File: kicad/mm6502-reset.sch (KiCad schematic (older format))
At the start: 19 parts, among them SW1 SW_Push, U1 W65C02SxP, U2 AT28C256, U3 62256, U4 W65C22SxP, U5 74HC00, U5 LM555, X1 1MHz

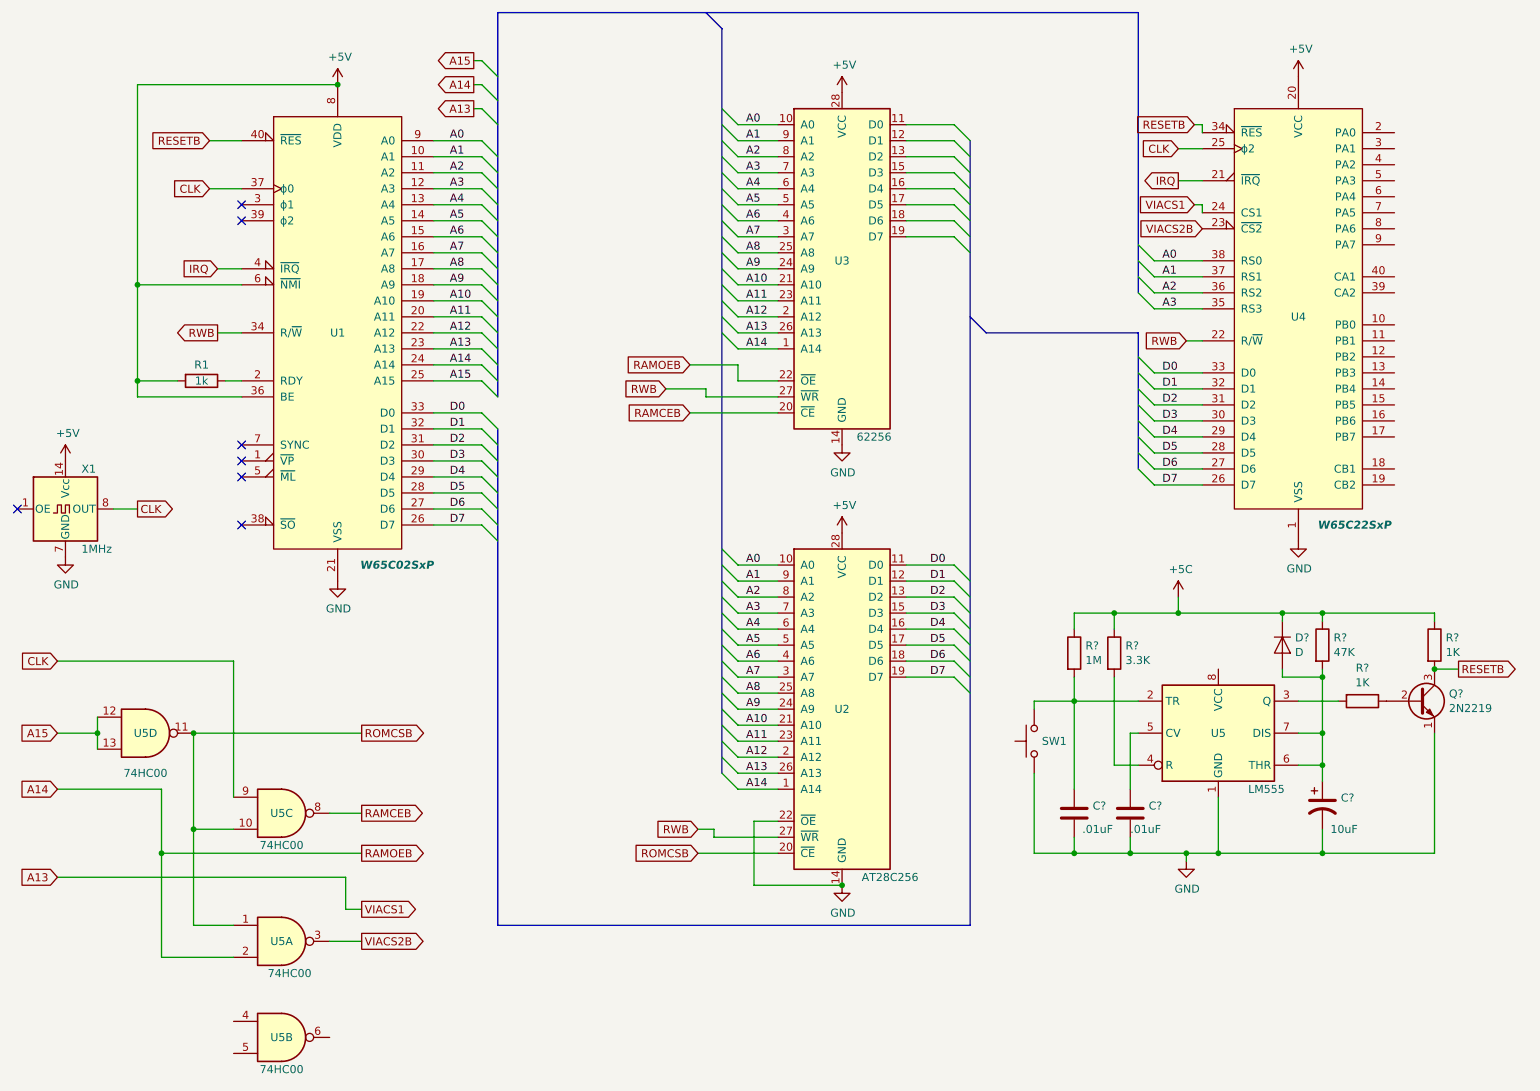
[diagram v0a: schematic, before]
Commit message: Add reset circuit
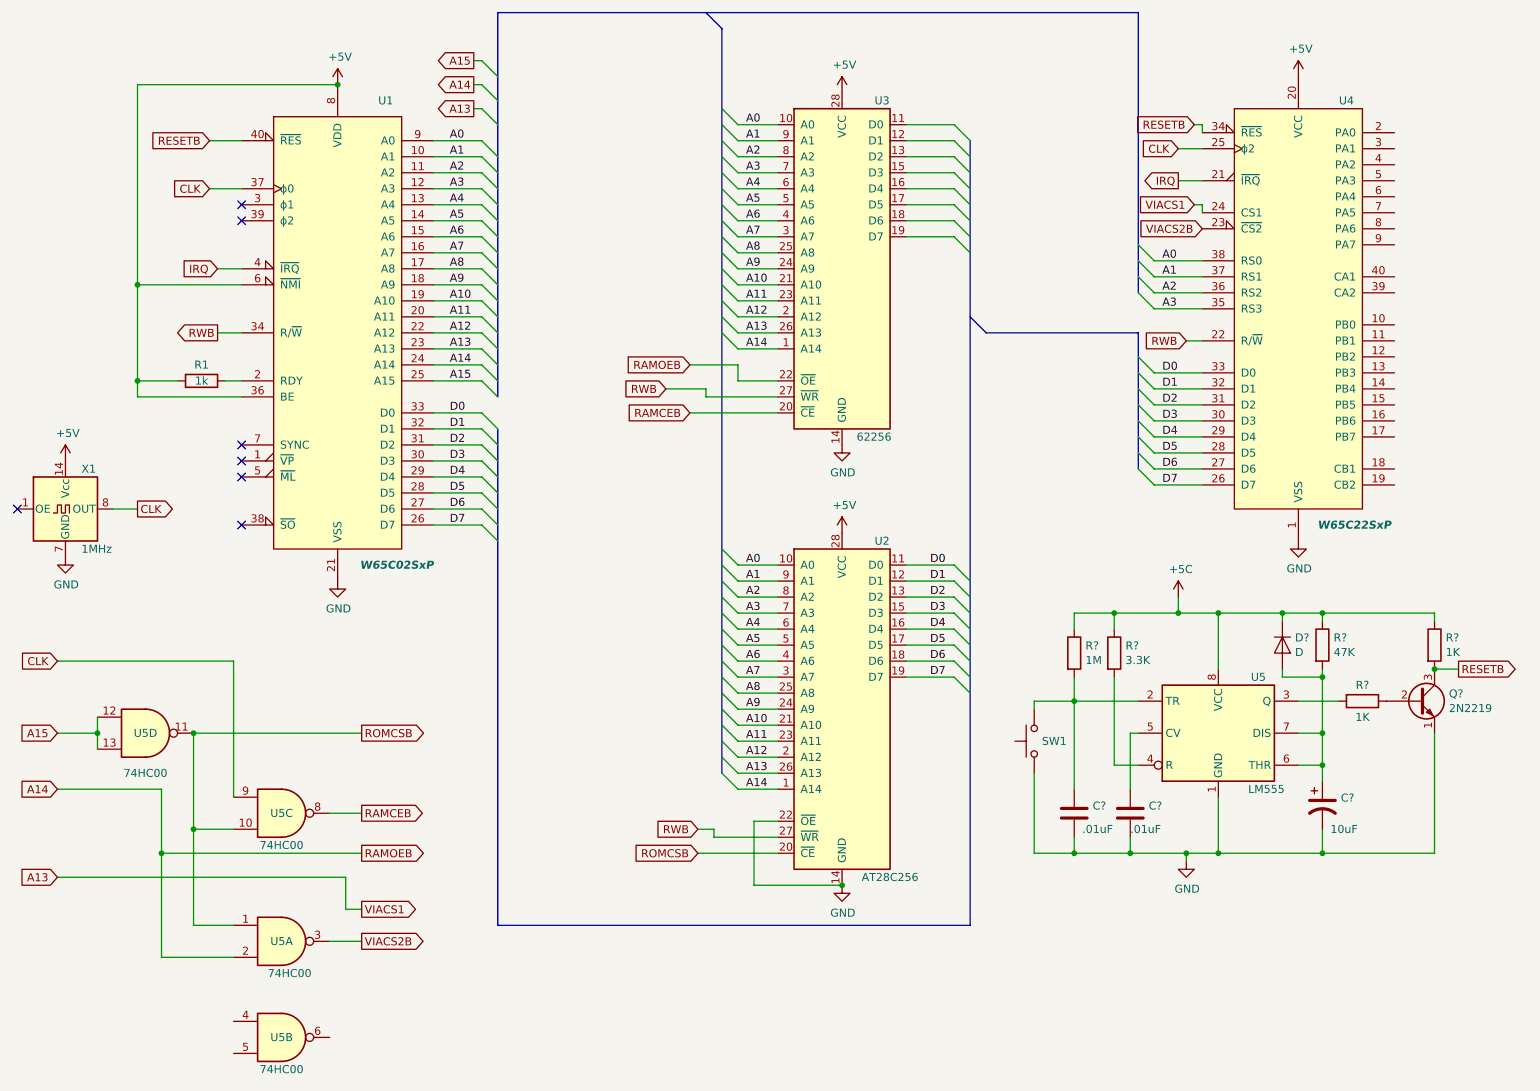
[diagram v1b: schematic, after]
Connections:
- net +5C: now also U5.8 (VCC)
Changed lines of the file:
@@
 U 1 1 63C25691
 P 6250 5250
-F 0 "U2" H 6250 5250 50  0000 C CNN
+F 0 "U2" H 6500 6300 50  0000 C CNN
 F 1 "AT28C256" H 6550 4200 50  0000 C CNN
 F 2 "" H 6250 5250 50  0001 C CNN
@@
 U 1 1 63C2336B
 P 9100 2750
-F 0 "U4" H 9100 2700 50  0000 C CNN
+F 0 "U4" H 9400 4050 50  0000 C CNN
 F 1 "W65C22SxP" H 9450 1400 50  0000 C CIB
 F 2 "" H 9100 2900 50  0001 C CNN
@@
 U 1 1 63C274DB
 P 6250 2500
-F 0 "U3" H 6250 2550 50  0000 C CNN
+F 0 "U3" H 6500 3550 50  0000 C CNN
 F 1 "62256" H 6450 1450 50  0000 C CNN
 F 2 "" H 6250 2500 50  0001 C CNN
@@
 U 1 1 63C201B7
 P 3100 2900
-F 0 "U1" H 3100 2900 50  0000 C CNN
+F 0 "U1" H 3400 4350 50  0000 C CNN
 F 1 "W65C02SxP" H 3700 1450 50  0000 R CIB
 F 2 "" H 3100 4900 50  0001 C CNN
@@
 U 1 1 63CC6136
 P 8600 5400
-F 0 "U5" H 8600 5400 50  0000 C CNN
+F 0 "U5" H 8850 5750 50  0000 C CNN
 F 1 "LM555" H 8900 5050 50  0000 C CNN
 F 2 "" H 8600 5400 50  0001 C CNN
@@
 U 1 1 63CD04BA
 P 9500 5200
-F 0 "R?" V 9293 5200 50  0000 C CNN
-F 1 "1K" V 9384 5200 50  0000 C CNN
+F 0 "R?" V 9400 5200 50  0000 C CNN
+F 1 "1K" V 9600 5200 50  0000 C CNN
 F 2 "" V 9430 5200 50  0001 C CNN
 F 3 "~" H 9500 5200 50  0001 C CNN
@@
 Connection ~ 8350 4650
 Wire Wire Line
-	8350 4650 9000 4650
+	8350 4650 8600 4650
 Wire Wire Line
 	9000 4700 9000 4650
@@
 	10100 5000 9950 5000
 Connection ~ 9950 5000
+Wire Wire Line
+	8600 5000 8600 4650
 Wire Bus Line
 	4100 900  8100 900
@@
 Wire Bus Line
 	5500 1000 5500 5650
+Connection ~ 8600 4650
+Wire Wire Line
+	8600 4650 9000 4650
 $EndSCHEMATC

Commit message: Multiple sheets
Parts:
- removed R1: 1k, symbol Device:R
- removed U1: W65C02SxP, symbol 65xx:W65C02SxP
- removed U2: AT28C256, symbol 8bits:AT28C256
- removed U3: 62256, symbol 8bits:62256
- removed U4: W65C22SxP, symbol 65xx:W65C22SxP
- removed U5: 74HC00, symbol 74xx:74HC00
- removed unit 2 of U5
- removed unit 3 of U5
- removed unit 4 of U5
- removed X1: 1MHz, Oscillator:Oscillator_SeikoEpson_SG-8002DB, symbol Oscillator:SG-8002DB
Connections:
- no-connect marks 7 -> 0
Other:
- moved on the sheet: C?, D?, Q?, R?, SW1, U5

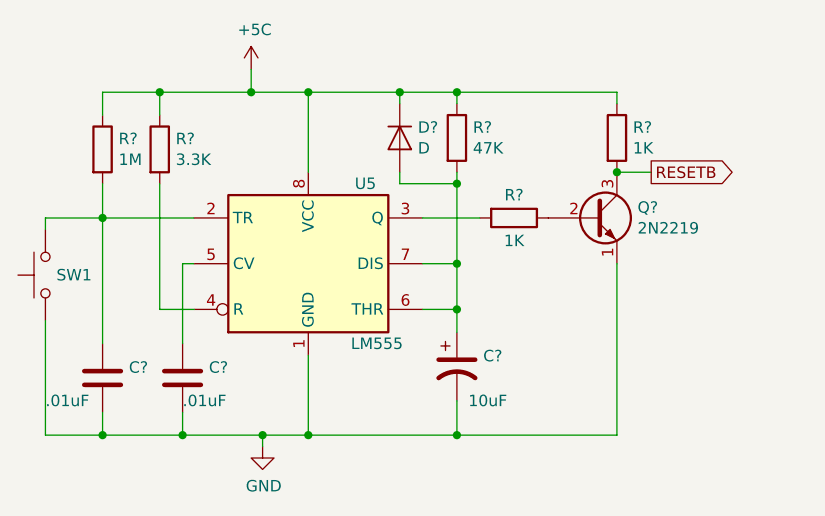
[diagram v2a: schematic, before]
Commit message: Set reference ids in reset circuit
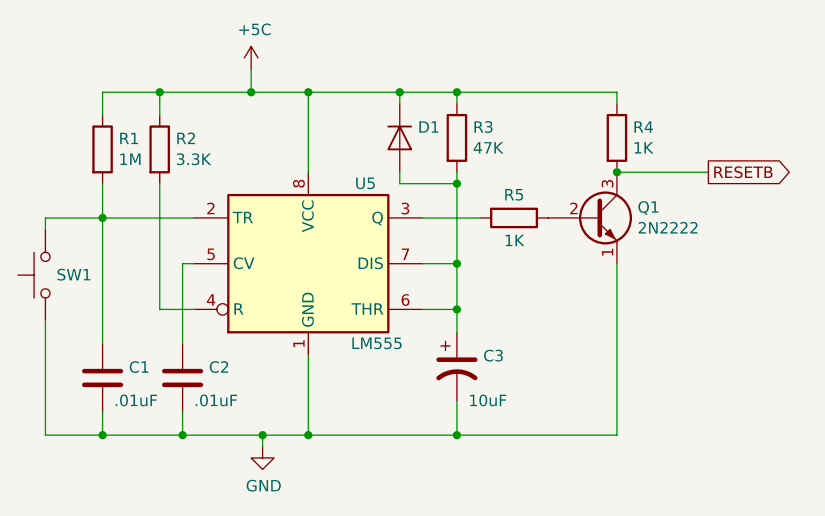
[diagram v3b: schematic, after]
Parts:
- Q1: renamed from Q?; value 2N2219 -> 2N2222
- gave numbers to parts that had none: 9
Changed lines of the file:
@@
 $EndComp
 $Comp
-L Device:C C?
+L Device:C C2
 U 1 1 63CCB368
 P 4500 4050
-F 0 "C?" H 4615 4096 50  0000 L CNN
-F 1 ".01uF" H 4500 3950 50  0000 L CNN
+F 0 "C2" H 4615 4096 50  0000 L CNN
+F 1 ".01uF" H 4550 3950 50  0000 L CNN
 F 2 "" H 4538 3900 50  0001 C CNN
 F 3 "~" H 4500 4050 50  0001 C CNN
@@
 $EndComp
 $Comp
-L Device:C C?
+L Device:C C1
 U 1 1 63CCB915
 P 4150 4050
-F 0 "C?" H 4265 4096 50  0000 L CNN
-F 1 ".01uF" H 3900 3950 50  0000 L CNN
+F 0 "C1" H 4265 4096 50  0000 L CNN
+F 1 ".01uF" H 4200 3950 50  0000 L CNN
 F 2 "" H 4188 3900 50  0001 C CNN
 F 3 "~" H 4150 4050 50  0001 C CNN
@@
 $EndComp
 $Comp
-L Device:CP1 C?
+L Device:CP1 C3
 U 1 1 63CCD72E
 P 5700 4000
-F 0 "C?" H 5815 4046 50  0000 L CNN
+F 0 "C3" H 5815 4046 50  0000 L CNN
 F 1 "10uF" H 5750 3850 50  0000 L CNN
 F 2 "" H 5700 4000 50  0001 C CNN
@@
 $EndComp
 $Comp
-L Device:R R?
+L Device:R R1
 U 1 1 63CCDE38
 P 4150 3050
-F 0 "R?" H 4220 3096 50  0000 L CNN
+F 0 "R1" H 4220 3096 50  0000 L CNN
 F 1 "1M" H 4220 3005 50  0000 L CNN
 F 2 "" V 4080 3050 50  0001 C CNN
@@
 $EndComp
 $Comp
-L Device:R R?
+L Device:R R2
 U 1 1 63CCE3FD
 P 4400 3050
-F 0 "R?" H 4470 3096 50  0000 L CNN
+F 0 "R2" H 4470 3096 50  0000 L CNN
 F 1 "3.3K" H 4470 3005 50  0000 L CNN
 F 2 "" V 4330 3050 50  0001 C CNN
@@
 $EndComp
 $Comp
-L Device:R R?
+L Device:R R3
 U 1 1 63CCF1C3
 P 5700 3000
-F 0 "R?" H 5770 3046 50  0000 L CNN
+F 0 "R3" H 5770 3046 50  0000 L CNN
 F 1 "47K" H 5770 2955 50  0000 L CNN
 F 2 "" V 5630 3000 50  0001 C CNN
@@
 $EndComp
 $Comp
-L Device:D D?
+L Device:D D1
 U 1 1 63CCFA0D
 P 5450 3000
-F 0 "D?" V 5404 3079 50  0000 L CNN
-F 1 "D" V 5495 3079 50  0000 L CNN
+F 0 "D1" V 5404 3079 50  0000 L CNN
+F 1 "D" V 5495 3079 50  0001 L CNN
 F 2 "" H 5450 3000 50  0001 C CNN
 F 3 "~" H 5450 3000 50  0001 C CNN
@@
 $EndComp
 $Comp
-L Device:R R?
+L Device:R R4
 U 1 1 63CD0046
 P 6400 3000
-F 0 "R?" H 6470 3046 50  0000 L CNN
+F 0 "R4" H 6470 3046 50  0000 L CNN
 F 1 "1K" H 6470 2955 50  0000 L CNN
 F 2 "" V 6330 3000 50  0001 C CNN
@@
 $EndComp
 $Comp
-L Device:R R?
+L Device:R R5
 U 1 1 63CD04BA
 P 5950 3350
-F 0 "R?" V 5850 3350 50  0000 C CNN
+F 0 "R5" V 5850 3350 50  0000 C CNN
 F 1 "1K" V 6050 3350 50  0000 C CNN
 F 2 "" V 5880 3350 50  0001 C CNN
@@
 $EndComp
 $Comp
-L Transistor_BJT:2N2219 Q?
+L Transistor_BJT:2N2219 Q1
 U 1 1 63CD1756
 P 6300 3350
-F 0 "Q?" H 6490 3396 50  0000 L CNN
-F 1 "2N2219" H 6490 3305 50  0000 L CNN
+F 0 "Q1" H 6490 3396 50  0000 L CNN
+F 1 "2N2222" H 6490 3305 50  0000 L CNN
 F 2 "Package_TO_SOT_THT:TO-39-3" H 6500 3275 50  0001 L CIN
 F 3 "http://www.onsemi.com/pub_link/Collateral/2N2219-D.PDF" H 6300 3350 50  0001 L CNN
@@
 Wire Wire Line
 	5550 3350 5800 3350
-Text GLabel 6550 3150 2    50   Output ~ 0
+Text GLabel 6800 3150 2    50   Output ~ 0
 RESETB
-Wire Wire Line
-	6550 3150 6400 3150
 Connection ~ 6400 3150
 Wire Wire Line
@@
 Wire Wire Line
 	5050 2800 5450 2800
+Wire Wire Line
+	6400 3150 6800 3150
 $EndSCHEMATC
